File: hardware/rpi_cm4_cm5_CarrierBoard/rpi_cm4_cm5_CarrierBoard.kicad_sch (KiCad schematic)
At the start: 22 parts, among them J21 61300311121, J22 61300311121, J24 SM04B-SRSS-TB, U37 SN74LVC1G14DBVR

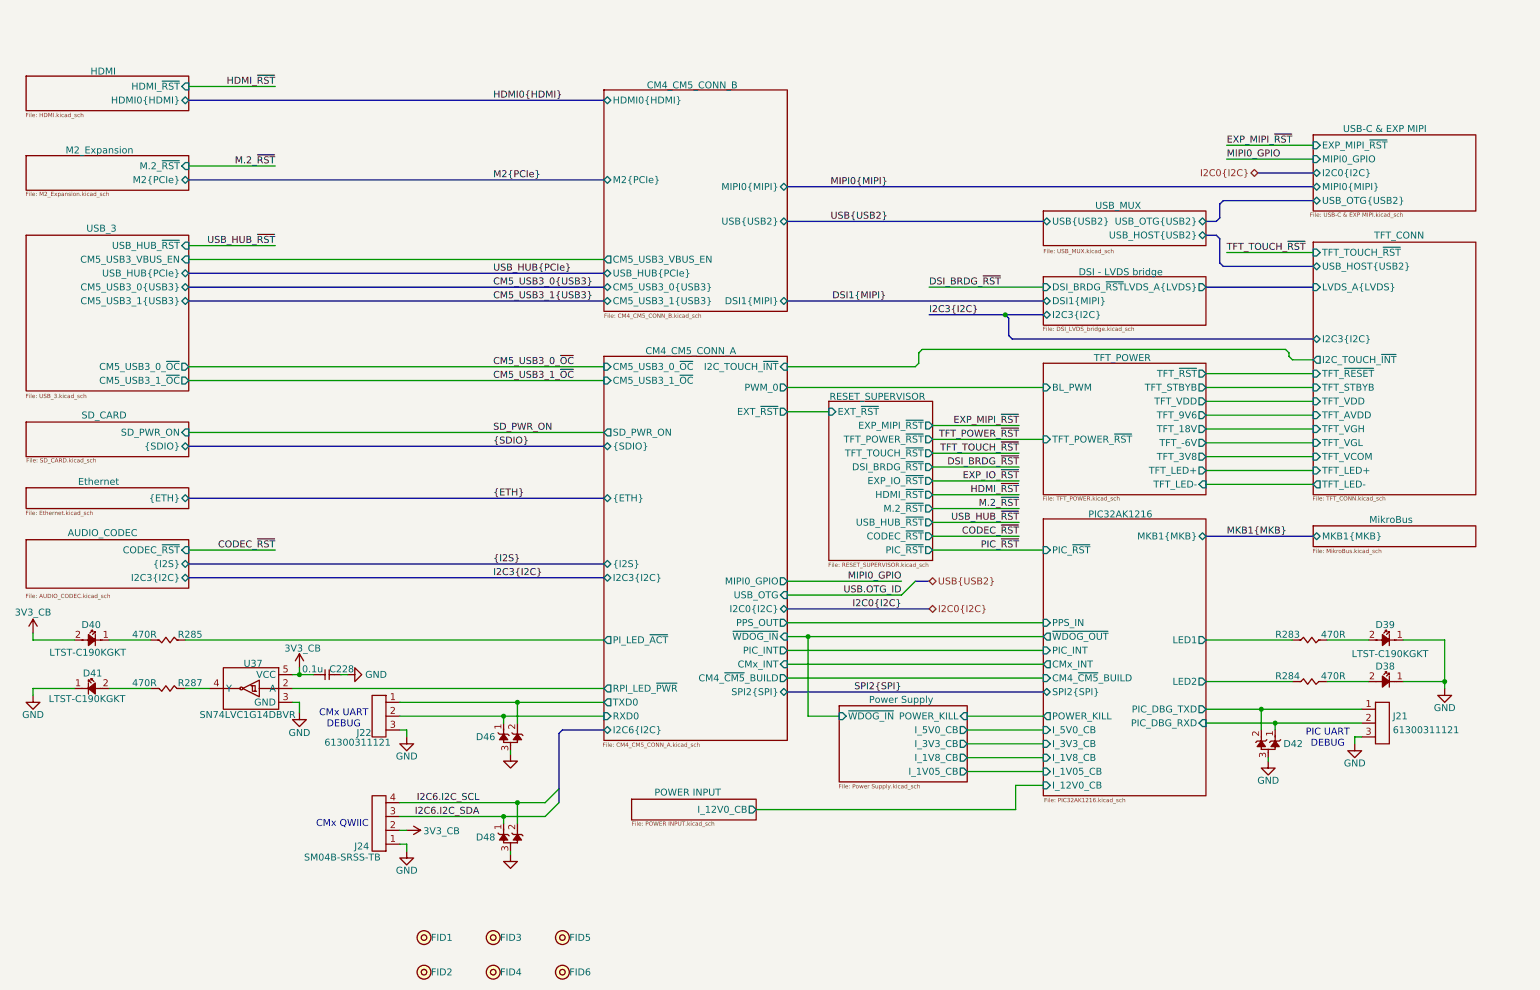
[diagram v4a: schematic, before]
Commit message: Cosmetic adjustments to schematics
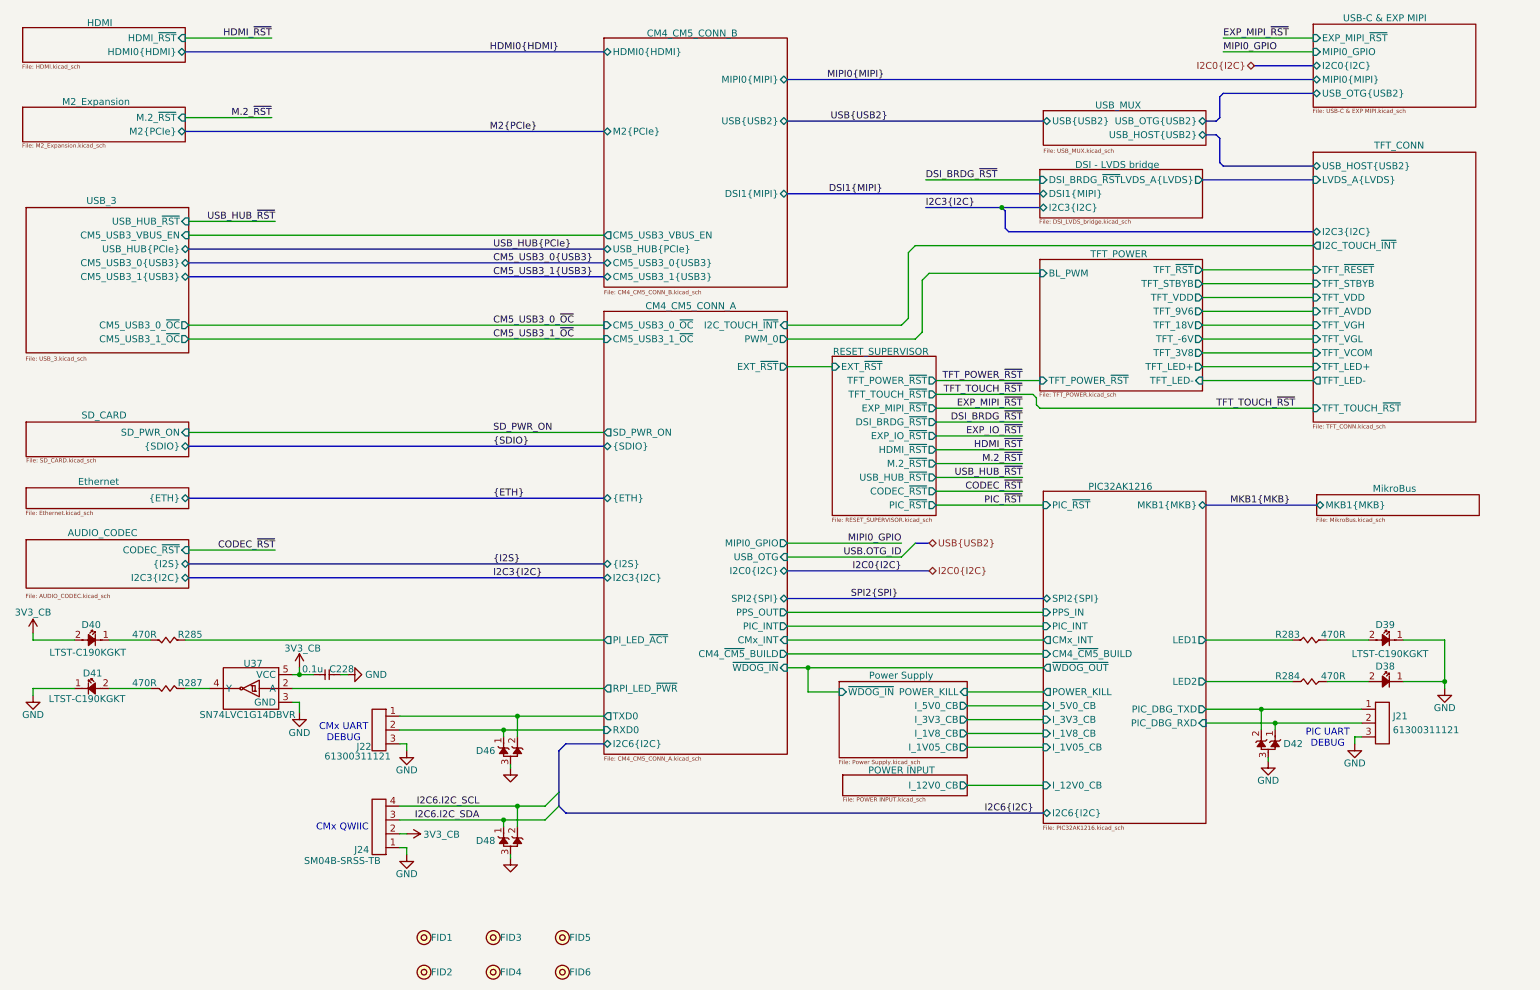
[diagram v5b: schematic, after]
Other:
- sheet PIC32AK1216 ports: added I2C6{I2C}; removed none
- moved on the sheet: D46, D48, J22, J24

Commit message: Continue working on the layout. Completed most of power planes planning and pouring Completed all DiffPairs routing and length matching (preliminary)
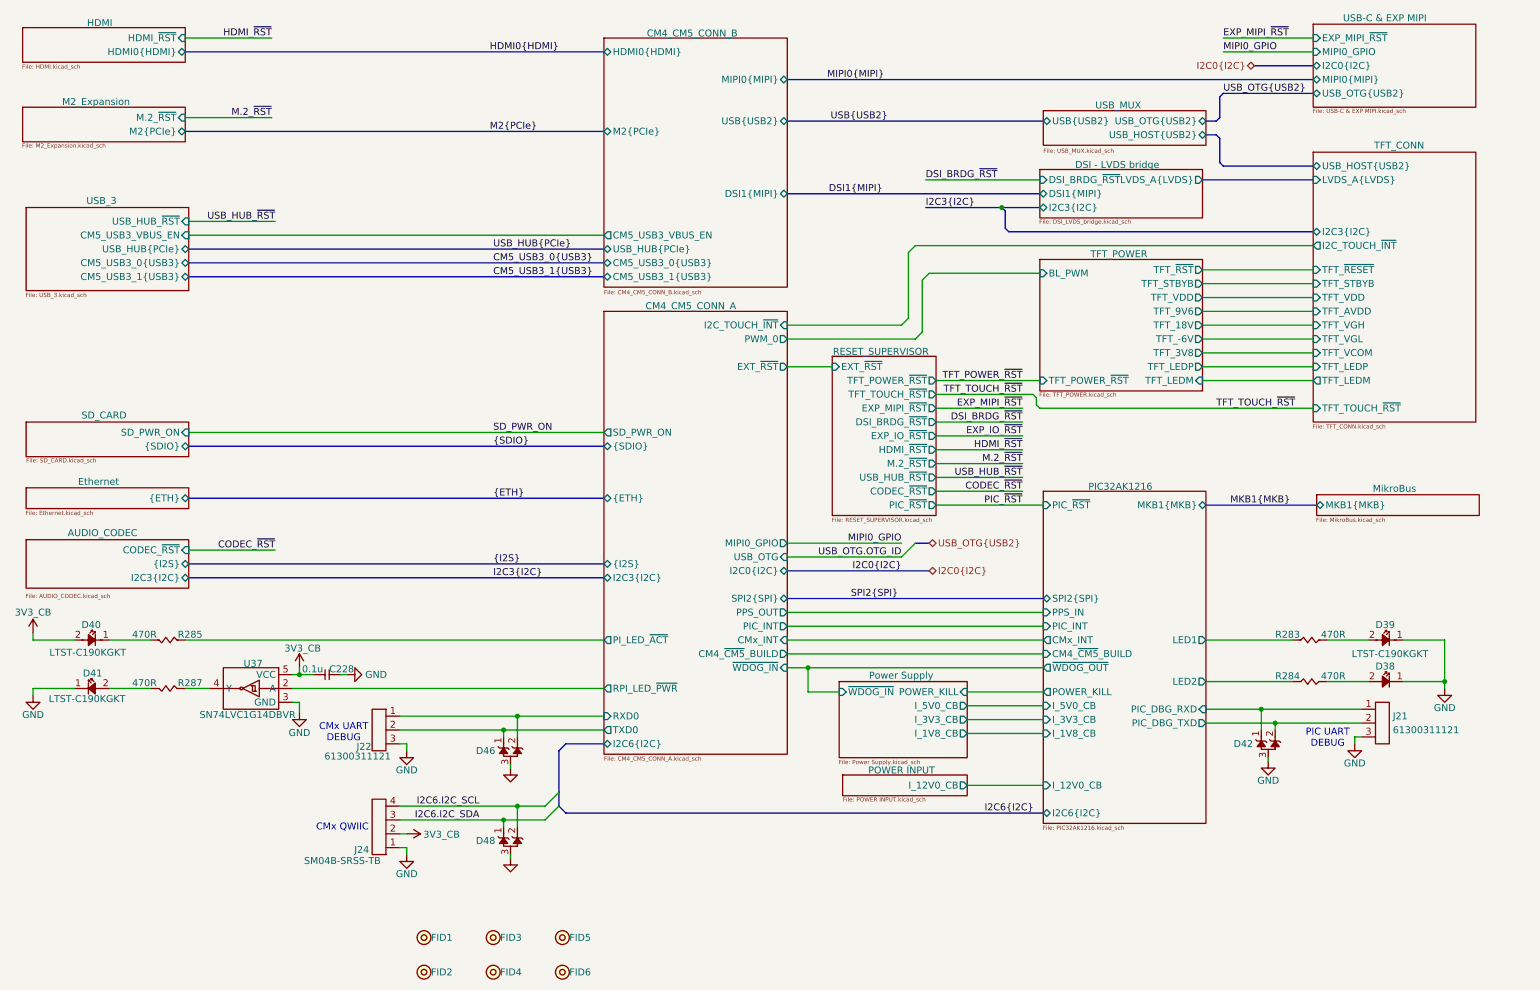
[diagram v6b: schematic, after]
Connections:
- net CM4_CM5_CONN_A/RXD0: now also D46.2 (A), J22.1; no longer D46.1, J22.2
- net CM4_CM5_CONN_A/TXD0: now also D46.1, J22.2; no longer D46.2 (A), J22.1
- net PIC32AK1216/PIC_DBG_RXD: now also J21.1; no longer J21.2
- net PIC32AK1216/PIC_DBG_TXD: now also J21.2; no longer J21.1
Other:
- sheet CM4_CM5_CONN_A ports: added none; removed CM5_USB3_0_~{OC}, CM5_USB3_1_~{OC}
- sheet PIC32AK1216 ports: added none; removed I_1V05_CB
- sheet Power Supply ports: added none; removed I_1V05_CB
- sheet TFT_CONN ports: added TFT_LEDM, TFT_LEDP; removed TFT_LED+, TFT_LED-
- sheet TFT_POWER ports: added TFT_LEDM, TFT_LEDP; removed TFT_LED+, TFT_LED-
- sheet USB_3 ports: added none; removed CM5_USB3_0_~{OC}, CM5_USB3_1_~{OC}

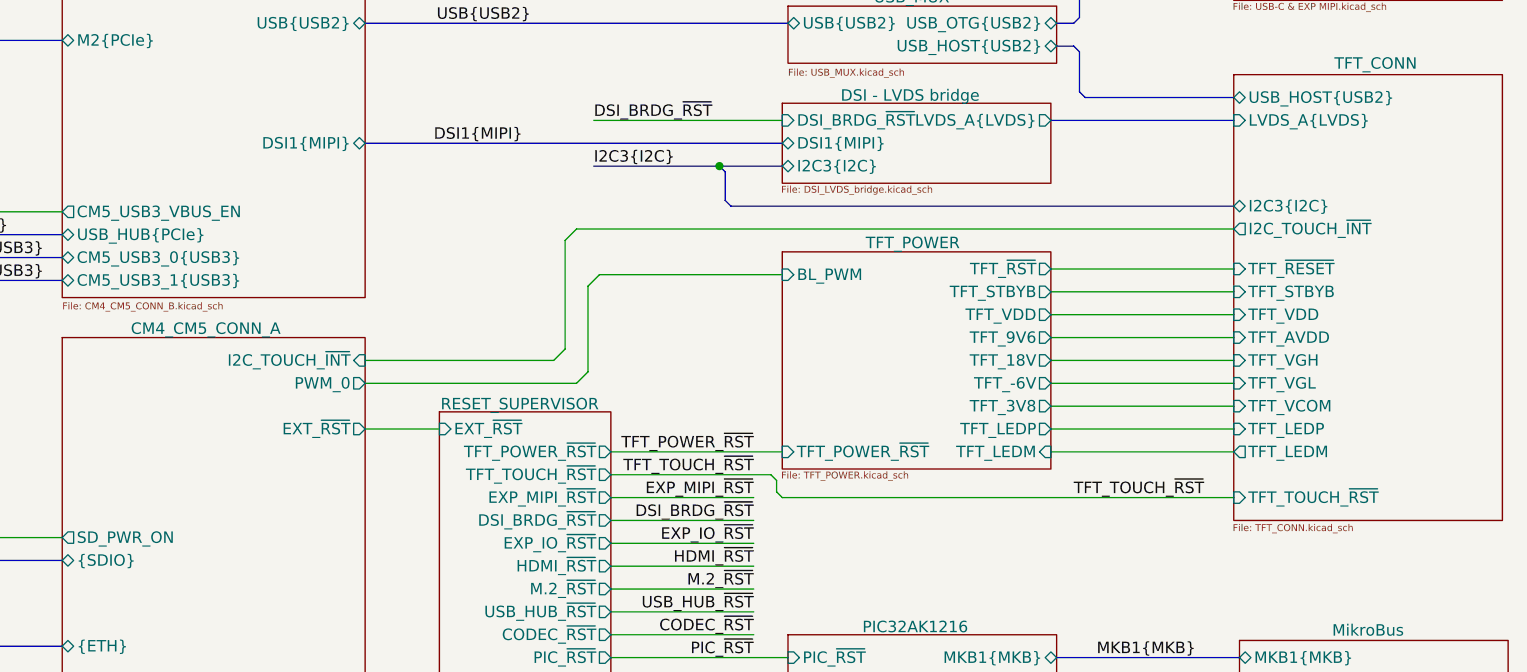
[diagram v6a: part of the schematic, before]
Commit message: Significant update Stackup changed from 6 to 8 layers Changed design notes accordingly Re-routed all differential pairs and length match / skew match Fanout critical signals away from dense areas 95% routing completed
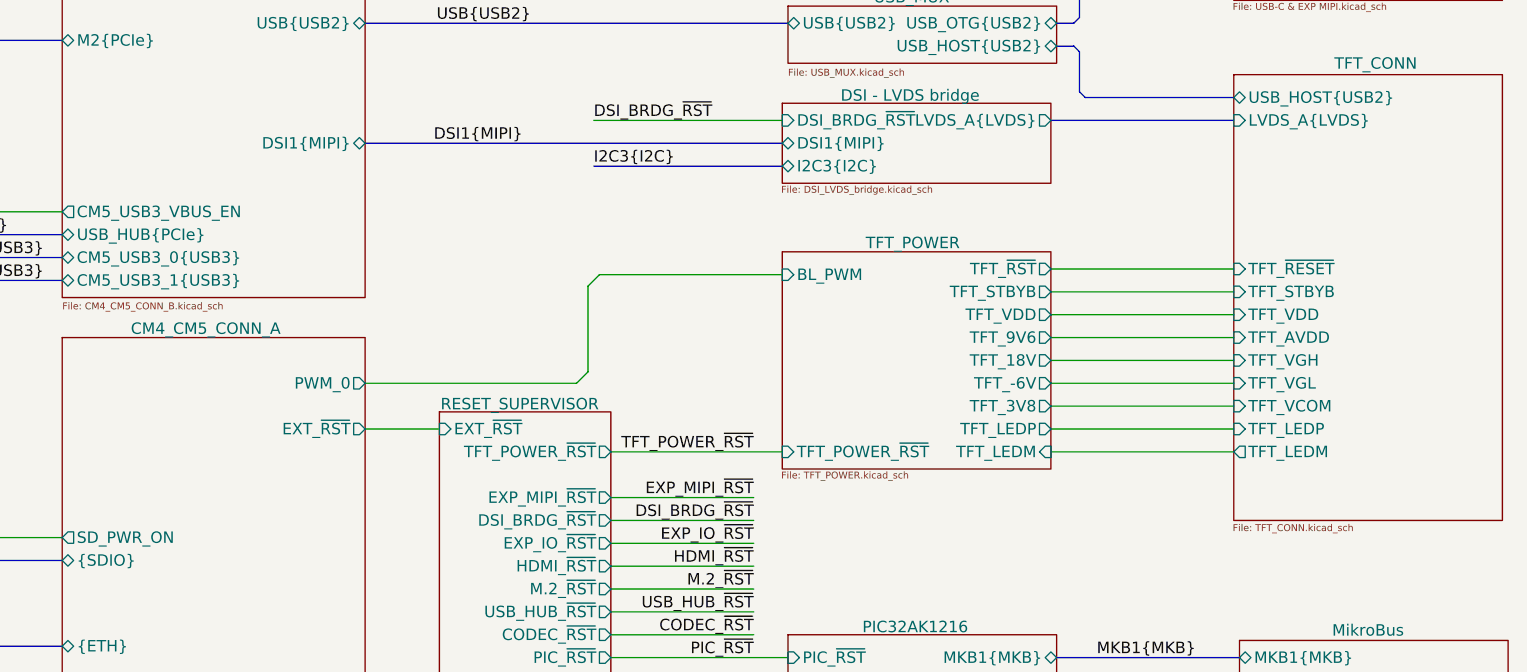
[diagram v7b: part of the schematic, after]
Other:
- sheet CM4_CM5_CONN_A ports: added none; removed I2C_TOUCH_~{INT}
- sheet RESET_SUPERVISOR ports: added none; removed TFT_TOUCH_~{RST}
- sheet TFT_CONN ports: added none; removed I2C3{I2C}, I2C_TOUCH_~{INT}, TFT_TOUCH_~{RST}
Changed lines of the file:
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@@
 	(title_block
 		(title "RPI CMx Carrier")
-		(date "2026-01-22")
+		(date "2026-02-13")
 		(rev "2.00-0A")
 		(comment 1 "Jean-Francois Bilodeau")
@@
 	)
 	(junction
-		(at 194.945 50.165)
-		(diameter 0)
-		(color 0 0 0 0)
-	)
-	(junction
 		(at 106.045 143.51)
 		(diameter 0)
@@
 	(bus
 		(pts
-			(xy 196.215 54.61) (xy 195.58 53.975)
-		)
-		(stroke
-			(width 0)
-			(type default)
-		)
-	)
-	(bus
-		(pts
-			(xy 194.945 50.165) (xy 201.93 50.165)
+			(xy 180.975 50.165) (xy 201.93 50.165)
 		)
 		(stroke
@@
 	(wire
 		(pts
-			(xy 179.07 57.15) (xy 252.095 57.15)
-		)
-		(stroke
-			(width 0)
-			(type default)
-		)
-	)
-	(wire
-		(pts
 			(xy 182.88 92.075) (xy 198.755 92.075)
 		)
@@
 	(wire
 		(pts
-			(xy 201.93 86.995) (xy 252.095 86.995)
-		)
-		(stroke
-			(width 0)
-			(type default)
-		)
-	)
-	(wire
-		(pts
 			(xy 182.88 102.235) (xy 198.755 102.235)
 		)
@@
 	(bus
 		(pts
-			(xy 180.975 50.165) (xy 194.945 50.165)
-		)
-		(stroke
-			(width 0)
-			(type default)
-		)
-	)
-	(bus
-		(pts
 			(xy 155.575 47.625) (xy 201.93 47.625)
 		)
@@
 	(wire
 		(pts
-			(xy 182.88 84.455) (xy 200.66 84.455)
-		)
-		(stroke
-			(width 0)
-			(type default)
-		)
-	)
-	(wire
-		(pts
 			(xy 155.575 129.54) (xy 202.565 129.54)
 		)
@@
 	(wire
 		(pts
-			(xy 155.575 71.755) (xy 176.53 71.755)
-		)
-		(stroke
-			(width 0)
-			(type default)
-		)
-	)
-	(wire
-		(pts
 			(xy 84.455 162.56) (xy 103.505 162.56)
 		)
@@
 	(wire
 		(pts
-			(xy 179.07 57.15) (xy 177.8 58.42)
-		)
-		(stroke
-			(width 0)
-			(type default)
-		)
-	)
-	(wire
-		(pts
 			(xy 188.595 141.605) (xy 202.565 141.605)
 		)
@@
 	(wire
 		(pts
-			(xy 201.295 86.36) (xy 201.93 86.995)
-		)
-		(stroke
-			(width 0)
-			(type default)
-		)
-	)
-	(wire
-		(pts
 			(xy 17.145 128.27) (xy 17.145 129.54)
 		)
@@
 	(bus
 		(pts
-			(xy 252.095 54.61) (xy 196.215 54.61)
-		)
-		(stroke
-			(width 0)
-			(type default)
-		)
-	)
-	(bus
-		(pts
 			(xy 121.92 148.59) (xy 114.935 148.59)
 		)
@@
 	(wire
 		(pts
-			(xy 200.66 84.455) (xy 201.295 85.09)
-		)
-		(stroke
-			(width 0)
-			(type default)
-		)
-	)
-	(wire
-		(pts
 			(xy 180.34 63.5) (xy 181.61 62.23)
 		)
@@
 		)
 	)
-	(bus
-		(pts
-			(xy 195.58 50.8) (xy 195.58 53.975)
-		)
-		(stroke
-			(width 0)
-			(type default)
-		)
-	)
 	(wire
 		(pts
@@
 	(wire
 		(pts
-			(xy 201.295 85.09) (xy 201.295 86.36)
-		)
-		(stroke
-			(width 0)
-			(type default)
-		)
-	)
-	(wire
-		(pts
 			(xy 155.575 132.08) (xy 202.565 132.08)
 		)
@@
 		)
 	)
-	(wire
-		(pts
-			(xy 177.8 58.42) (xy 177.8 70.485)
-		)
-		(stroke
-			(width 0)
-			(type default)
-		)
-	)
 	(bus
 		(pts
@@
 	(bus
 		(pts
-			(xy 195.58 50.8) (xy 194.945 50.165)
-		)
-		(stroke
-			(width 0)
-			(type default)
-		)
-	)
-	(bus
-		(pts
 			(xy 114.935 161.29) (xy 202.565 161.29)
 		)
@@
 	(wire
 		(pts
-			(xy 176.53 71.755) (xy 177.8 70.485)
-		)
-		(stroke
-			(width 0)
-			(type default)
-		)
-	)
-	(wire
-		(pts
 			(xy 103.505 146.05) (xy 121.92 146.05)
 		)
@@
 		)
 	)
-	(label "TFT_TOUCH_~{RST}"
-		(at 234.315 86.995 0)
-		(effects
-			(font
-				(size 1.27 1.27)
-			)
-			(justify left bottom)
-		)
-	)
 	(label "TFT_POWER_~{RST}"
 		(at 198.755 81.915 180)
@@
 		)
 	)
-	(label "TFT_TOUCH_~{RST}"
-		(at 198.755 84.455 180)
-		(effects
-			(font
-				(size 1.27 1.27)
-			)
-			(justify right bottom)
-		)
-	)
 	(label "SPI2{SPI}"
 		(at 175.895 121.92 180)
@@
 			)
 		)
-		(pin "I2C3{I2C}" bidirectional
-			(at 252.095 54.61 180)
-			(effects
-				(font
-					(size 1.27 1.27)
-				)
-				(justify left)
-			)
-		)
-		(pin "TFT_TOUCH_~{RST}" input
-			(at 252.095 86.995 180)
-			(effects
-				(font
-					(size 1.27 1.27)
-				)
-				(justify left)
-			)
-		)
-		(pin "I2C_TOUCH_~{INT}" output
-			(at 252.095 57.15 180)
-			(effects
-				(font
-					(size 1.27 1.27)
-				)
-				(justify left)
-			)
-		)
 		(pin "TFT_LEDP" input
 			(at 252.095 79.375 180)
@@
 			)
 		)
-		(pin "I2C_TOUCH_~{INT}" input
-			(at 155.575 71.755 0)
-			(effects
-				(font
-					(size 1.27 1.27)
-				)
-				(justify right)
-			)
-		)
 		(pin "I2C6{I2C}" bidirectional
 			(at 121.92 148.59 180)
@@
 			(effects
 				(font
-					(size 1.27 1.27)
-				)
-				(justify right)
-			)
-		)
-		(pin "TFT_TOUCH_~{RST}" output
-			(at 182.88 84.455 0)
-			(effects
-				(font
